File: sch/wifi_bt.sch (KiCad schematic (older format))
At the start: 3 parts, among them U1 AP6212

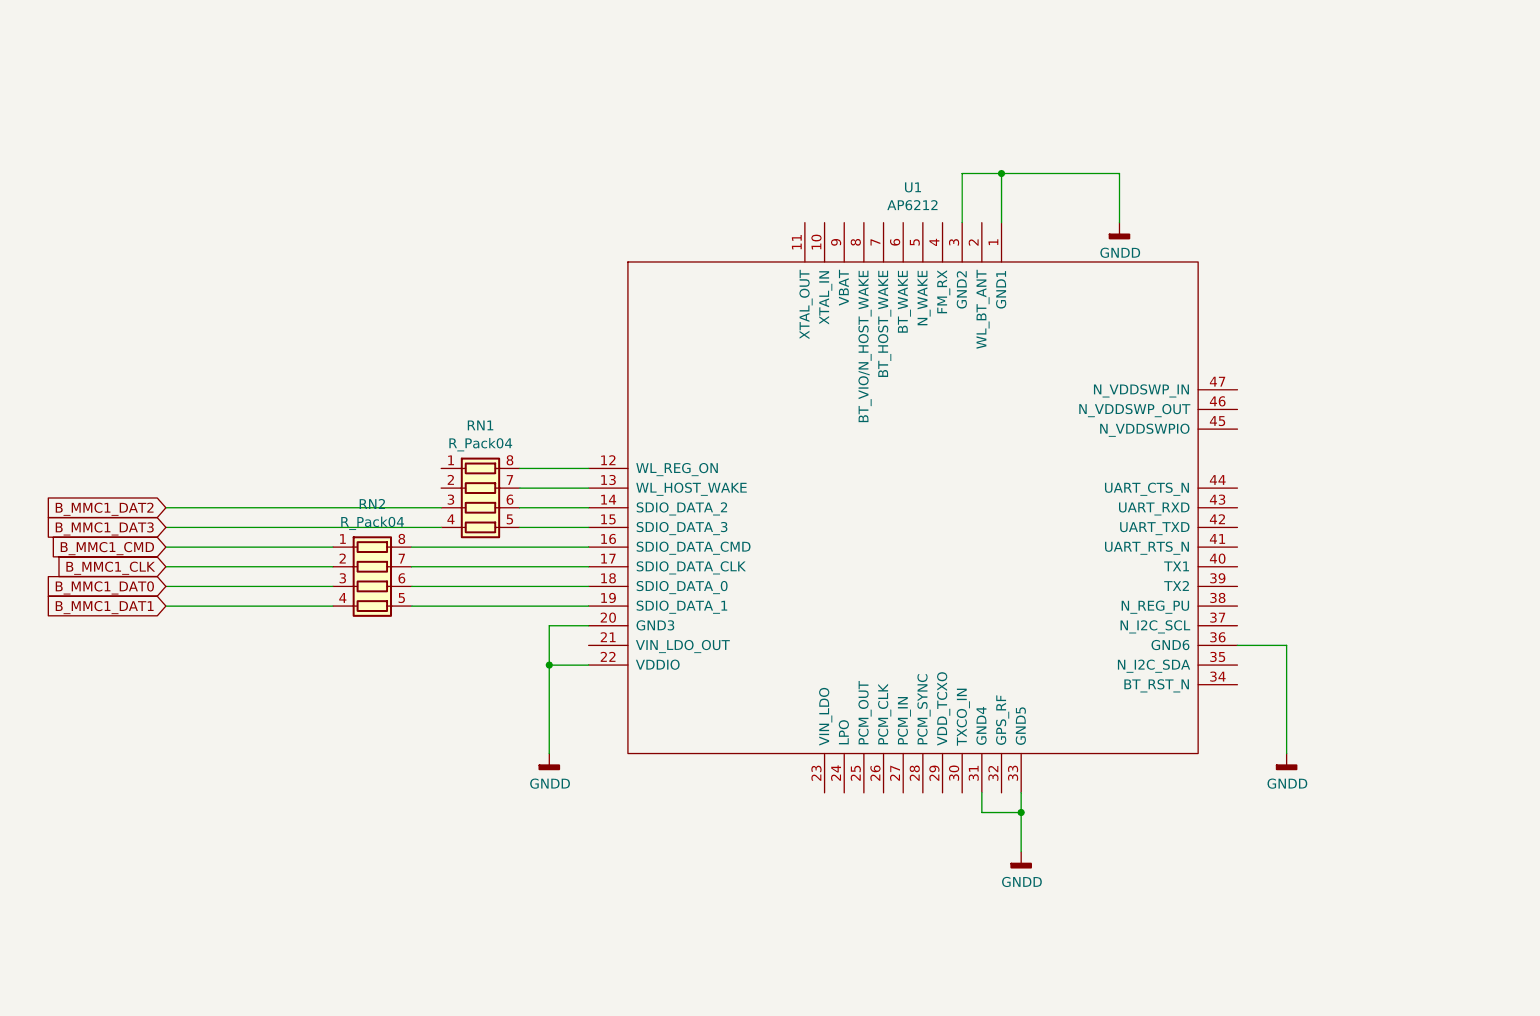
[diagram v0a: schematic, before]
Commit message: add u-boot sources
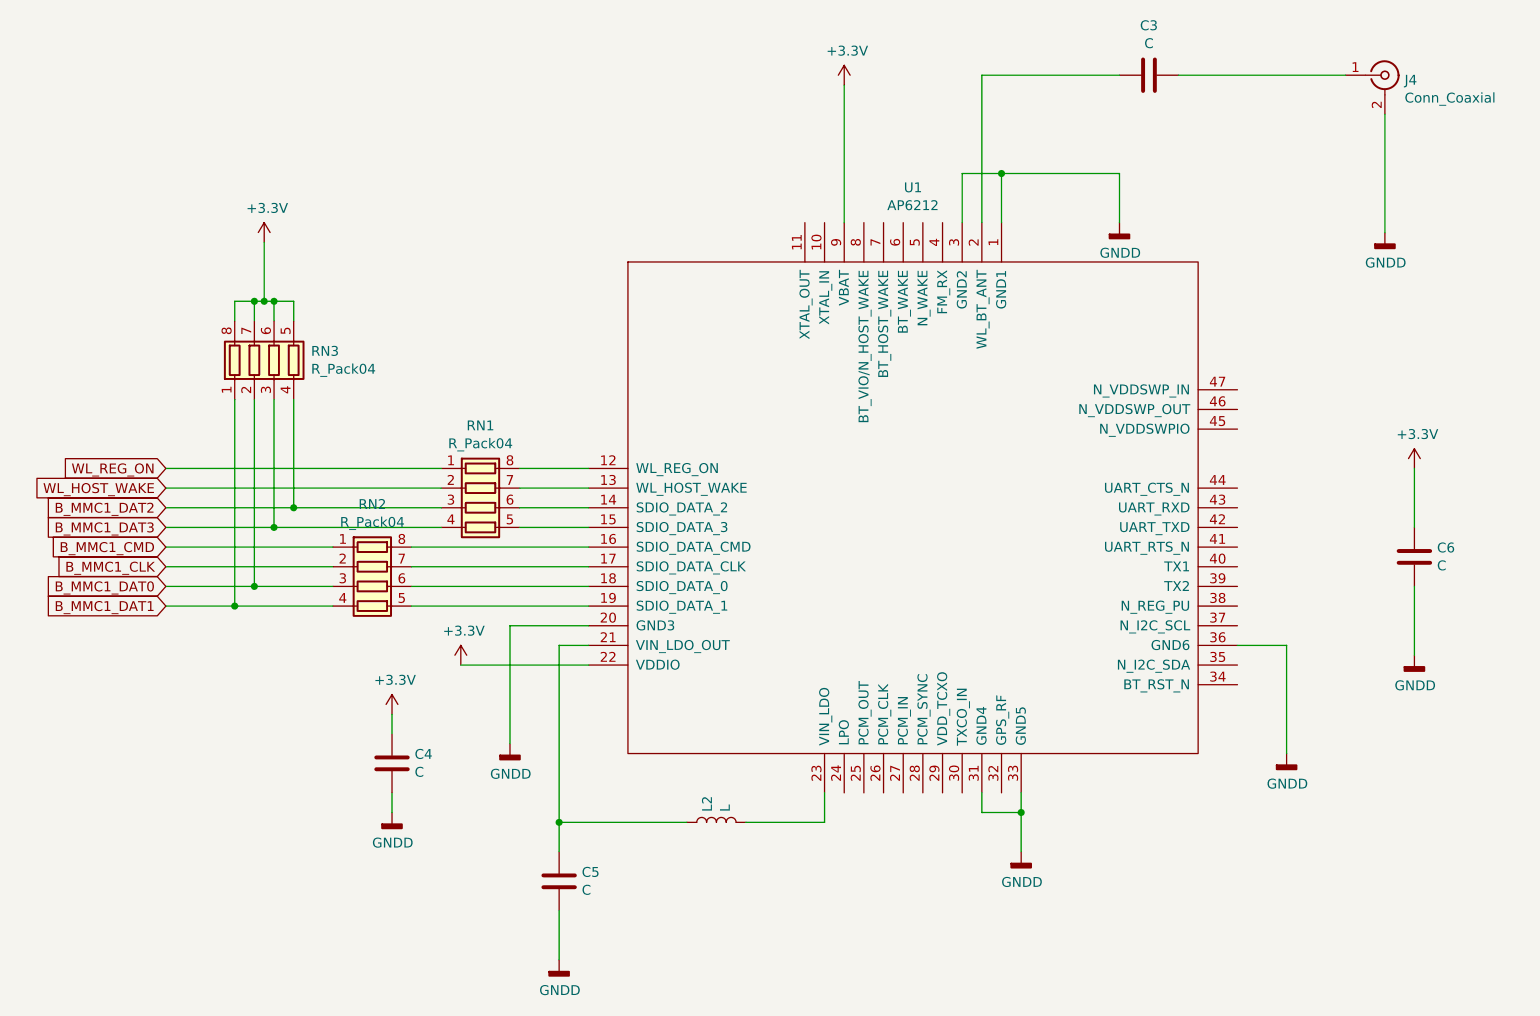
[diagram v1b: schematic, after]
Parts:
- added C3: C, Capacitor_SMD:C_0603_1608Metric, symbol Device:C
- added C4, C5, C6: C, Capacitor_SMD:C_0805_2012Metric, symbol Device:C
- added J4: Conn_Coaxial, Connector_Coaxial:U.FL_Molex_MCRF_73412-0110_Vertical, symbol Connector:Conn_Coaxial
- added L2: L, Inductor_SMD:L_1206_3216Metric, symbol Device:L
- added RN3: R_Pack04, Resistor_SMD:R_Array_Convex_4x0603, symbol Device:R_Pack04
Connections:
- net B_MMC1_DAT0: now also RN3.2 (R2.1)
- net B_MMC1_DAT1: now also RN3.1 (R1.1)
- net B_MMC1_DAT2: now also RN3.4 (R4.1)
- net B_MMC1_DAT3: now also RN3.3 (R3.1)
- net GNDD: now also C4.2, C5.2, C6.2, J4.2 (Ext); no longer U1.22 (VDDIO)
- net at U1.2 (WL_BT_ANT): now also C3.2
- net at U1.21 (VIN_LDO_OUT): now also C5.1, L2.1
- net at U1.23 (VIN_LDO): now also L2.2
- net +3V3: now reaches U1.9 (VBAT)
- net +3V3: now also U1.22 (VDDIO), C4.1, C6.1, RN3.5 (R4.2), RN3.6 (R3.2), RN3.7 (R2.2), RN3.8 (R1.2)
- net WL_REG_ON: now reaches RN1.1 (R1.1)
- net WL_HOST_WAKE: now reaches RN1.2 (R2.1)
- new net: C3.1, J4.1 (In)
